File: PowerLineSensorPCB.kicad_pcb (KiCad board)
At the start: 4 copper layers, 120 x 42.2 mm, 246 parts, among them IC1 SKY65943-11, IC2 BQ21080YBGR, J1 SIM_Card_Shielded, J10 Conn_Coaxial, J11 Conn_Coaxial, J12 Conn_Coaxial, J13 Conn_Coaxial, J14 Conn_01x06_Pin, J15 Conn_01x03_MountingPin, J16 Conn_01x03_MountingPin, J17 Conn_01x03_MountingPin, J2 Micro_SD_Card, J3 Conn_Coaxial, J5 Conn_01x04_Pin, J6 USB_C_Receptacle_USB2.0_16P, J7 Conn_Coaxial, J8 Conn_01x04_Pin, SW1 SW_Push, SW2 SW_Push, SW3 SW_Push, U11 LM2903, U12 W25Q128JVE, U13 W25Q128JVE, U3 RP2350A, U5 TMAG5253BAx, U6 nRF9151-LAXX, U7 LIS2HH12, U8 RAK3172-xx-8-SM-xI, Y1 Crystal_GND24

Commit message: Update PowerLineSensorPCB and nRF9151 schematic with designator adjustments and new GND symbol
- Modified the used designators in PowerLineSensorPCB to include an additional power reference.
- Renamed the sheet in PowerLineSensorPCB for clarity.
- Removed unnecessary junctions and adjusted wire connections in nRF9151 schematic for improved layout.
- Added a new GND symbol in nRF9151 schematic to create a global label for ground.
- Adjusted positions of several components and properties for better alignment and readability.
- Updated subproject commit reference for kicad-libs.
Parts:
- AE1: footprint robots4green:W3216 -> BC_RF:W3216
- ANT1: moved to B.Cu
- moved C32 221.2 mm to (236.1, 125.3)
- moved R131 221.2 mm to (236.1, 113.8)
- moved R138 221.2 mm to (266.4, 104.0)
- moved R60 221.2 mm to (245.7, 126.9)
- moved J1 191.0 mm to (183.2, 139.6), turned to 0 degrees
- moved R114 189.8 mm to (193.2, 127.3)
- moved R113 189.0 mm to (193.2, 123.4)
- moved R115 188.6 mm to (193.2, 126.3)
- moved C26 186.0 mm to (190.4, 130.3), turned to 90 degrees
- moved C28 183.5 mm to (189.4, 130.3), turned to 90 degrees
- moved C27 183.4 mm to (188.4, 130.3), turned to 90 degrees
- moved R121 182.9 mm to (193.2, 121.4)
- moved R122 182.5 mm to (193.2, 122.4)
- moved R123 182.5 mm to (193.2, 124.3)
- moved C41 181.7 mm to (172.2, 126.4), turned to 180 degrees
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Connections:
- C26 pad 2: Net-(C26-Pad2) -> GND
- C27 pad 2: Net-(C26-Pad2) -> GND
- C28 pad 2: Net-(C26-Pad2) -> GND
- C29 pad 2: Net-(C26-Pad2) -> GND
- C40 pad 2: Net-(C26-Pad2) -> GND
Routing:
- net GND: track 10.9 -> 0.01 mm
- net Net-(U8-RF): track 12.3 -> 6.51 mm
- net Net-(ANT1-FEED): track 14.1 -> 9.50 mm, vias 0 -> 1
- net Net-(C33-Pad1): track 3.25 -> 0.00 mm
- net Net-(J7-In): track 3.06 -> 0.00 mm
- net Net-(U6-ANT): track 2.31 -> 0.00 mm
- net Net-(D9-A2): track 18.3 -> 19.2 mm
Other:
- board size 120 x 42.2 mm -> 115 x 47 mm

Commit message: general improvments
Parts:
- removed C40: 4.7u, Capacitor_SMD:C_0402_1005Metric
- added R100: 100R, Resistor_SMD:R_0402_1005Metric, F.Cu at (125.2, 90.0)
- added R99: 100R, Resistor_SMD:R_0402_1005Metric, F.Cu at (130.1, 90.0)
- C24, C29, C31, C32, C36: value 4.7u -> 4u7; footprint Capacitor_SMD:C_0402_1005Metric -> Capacitor_SMD:C_1206_3216Metric
- C28: footprint Capacitor_SMD:C_0402_1005Metric -> Capacitor_SMD:C_1206_3216Metric
- U1: value ~ -> MLX90637
- U2: value ~ -> ZTPD2210
- U4: value ~ -> RT6150BGQW
- U9: value ~ -> P3T1755
- moved R90 96.2 mm to (162.6, 121.8)
- moved U9 82.1 mm to (141.8, 122.6), turned to 180 degrees
- moved R52 80.6 mm to (146.6, 123.8)
- moved R53 80.6 mm to (146.6, 122.8)
- moved C20 77.1 mm to (138.0, 123.0), turned to 90 degrees
- moved R50 25.9 mm to (165.0, 106.6), turned to 180 degrees
- moved R51 25.5 mm to (165.0, 105.4), turned to 180 degrees
- moved R21 9.88 mm to (88.4, 153.9)
- moved R25 9.88 mm to (91.3, 153.9)
- moved C21 9.88 mm to (85.5, 159.8)
- moved R20 9.88 mm to (88.4, 151.9)
- moved R22 9.88 mm to (88.4, 155.9)
- moved R23 9.88 mm to (88.4, 157.9)
- moved R24 9.88 mm to (91.3, 151.9)
- moved R26 9.88 mm to (91.3, 155.9)
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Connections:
- R16 pad 1: /50Hz -> Net-(R16-Pad1)
- R25 pad 1: /50Hz -> Net-(R16-Pad1)
- U11 pad 1: /50Hz -> Net-(R16-Pad1)
- U6 pad 53: /Celluar_GNSS/PPS -> Net-(U6-COEX1)
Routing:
- net /I2C0.SDA: track 0.00 -> 58.6 mm, vias 0 -> 3
- net /I2C0.SCL: track 0.00 -> 33.8 mm
- net Net-(U9-A0): track 0.00 -> 6.80 mm
- net Net-(U2-SDA): track 0.00 -> 5.46 mm
- net Net-(U2-SCL): track 0.00 -> 5.17 mm
- net Net-(U9-SCL): track 0.00 -> 2.19 mm
- net Net-(U1-SCL): track 0.00 -> 1.33 mm
- net Net-(U1-SDA): track 0.00 -> 1.29 mm

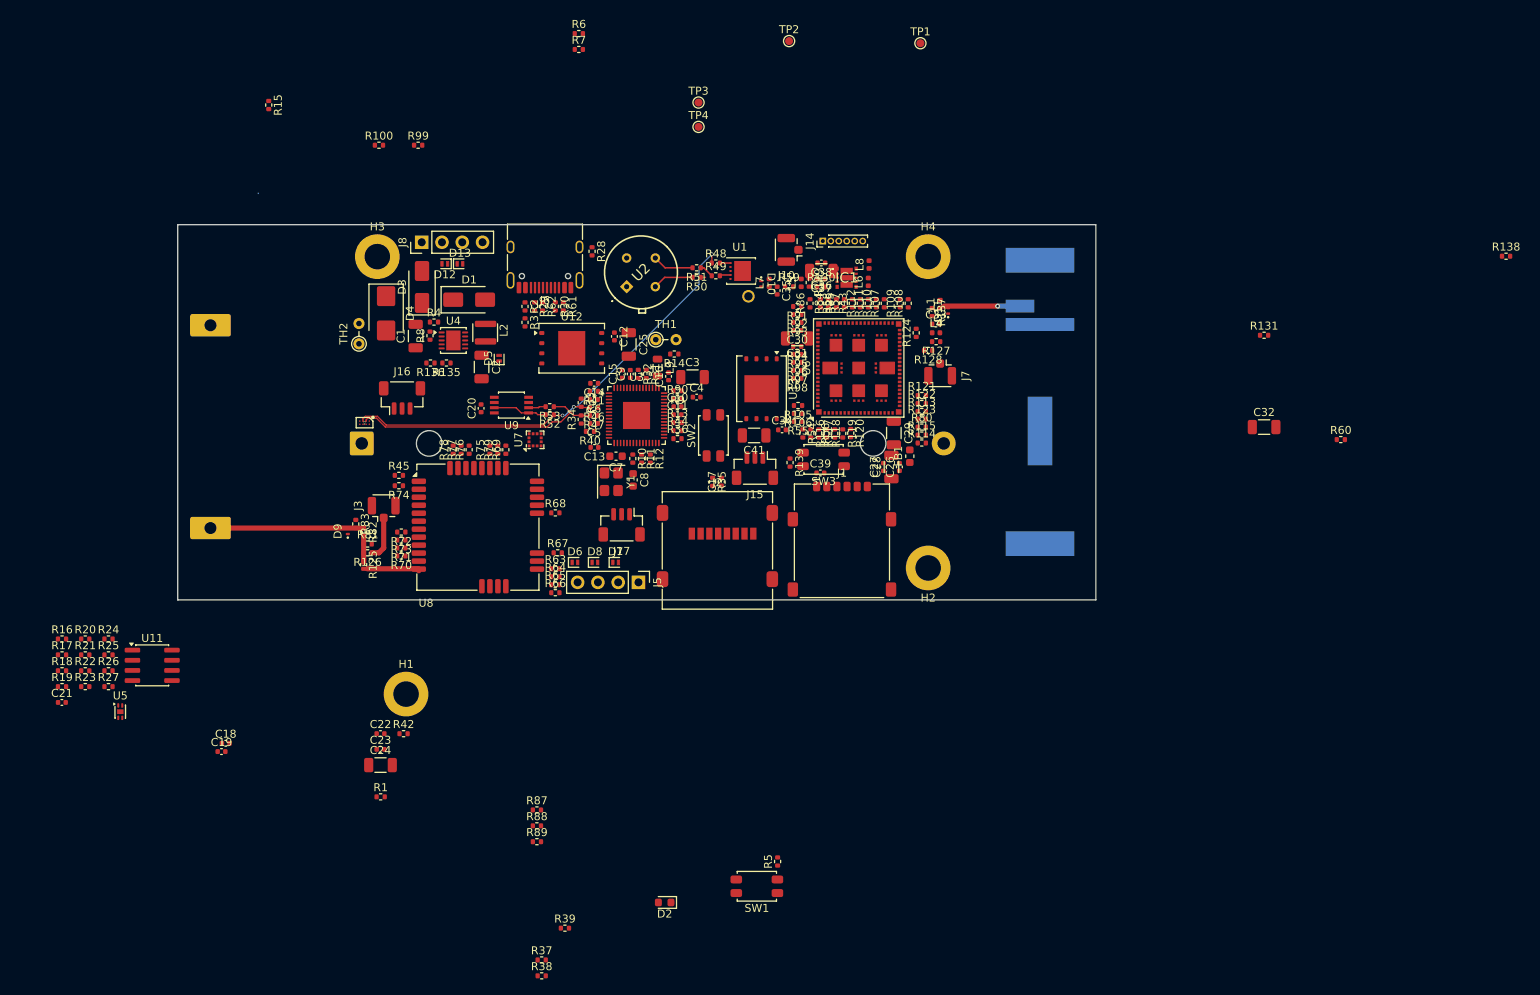
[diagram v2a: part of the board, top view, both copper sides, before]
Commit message: PCB routing.
Add netclass flags for power and signal in various schematics; update capacitor footprints and part numbers

- Introduced multiple netclass flags for "Power" and "Signal" in USB_Power, hall_effect_sensor, and nRF9151 schematics to enhance clarity and organization.
- Updated capacitor footprints from "C_1206_3216Metric" to "C_0402_1005Metric" and part numbers from "1206B475K500NT" to "CL05A475MP5NRNC" in accelerometer and nRF9151 schematics for consistency and accuracy.
- Updated submodule reference in kicad-libs to ensure compatibility with the latest library changes.
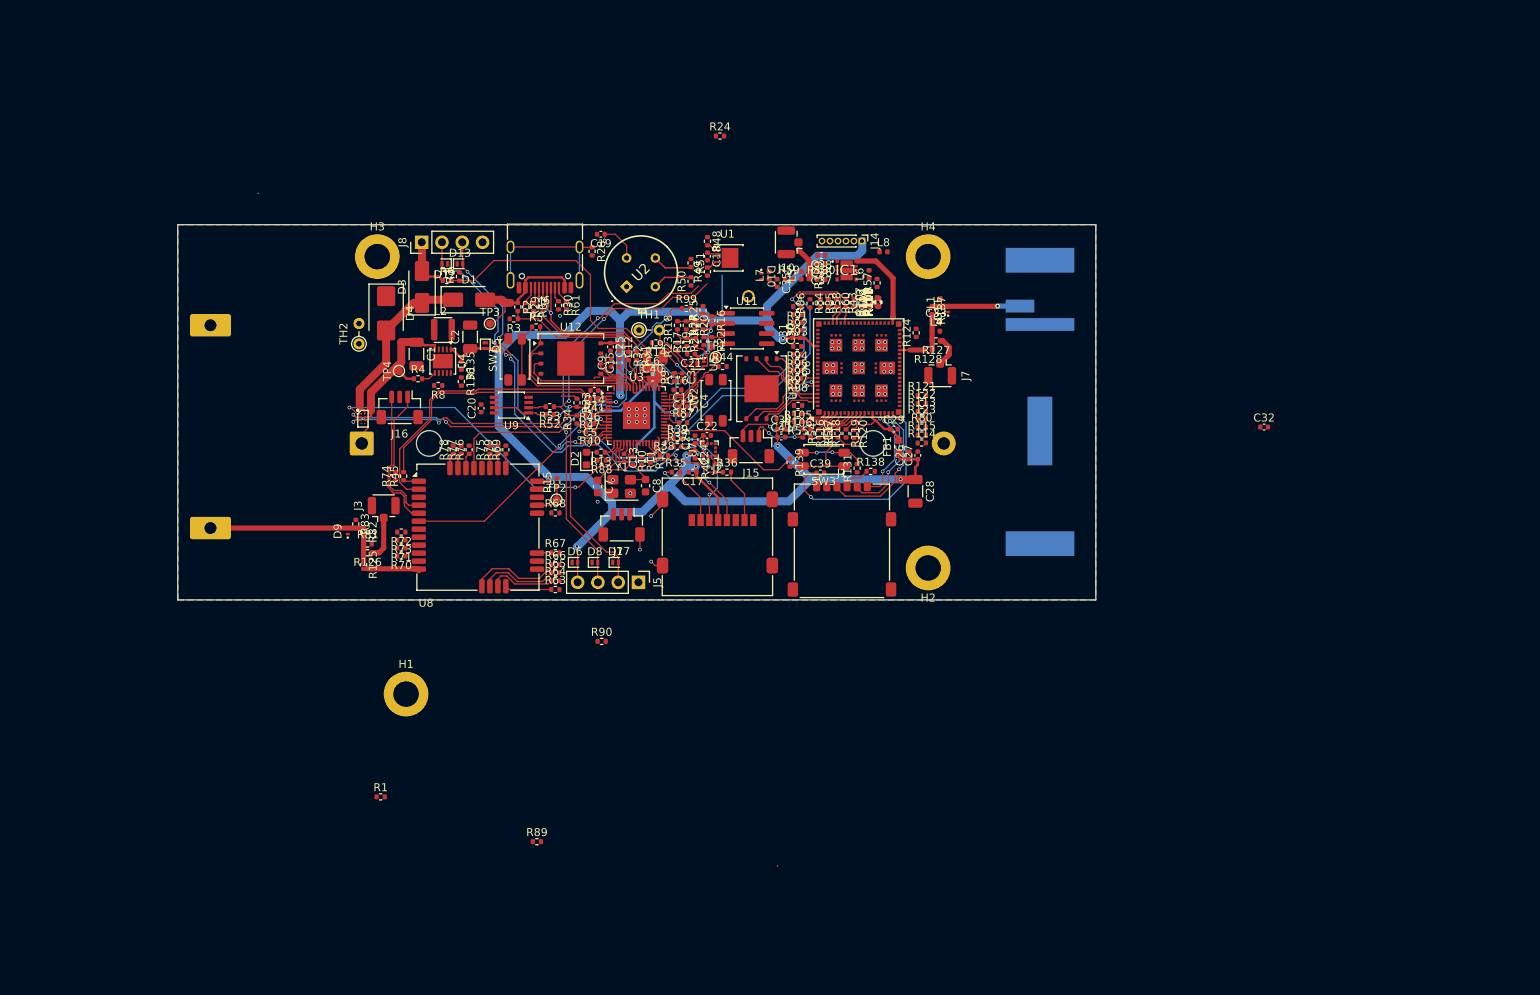
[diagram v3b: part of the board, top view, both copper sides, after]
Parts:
- added C40: 4u7, Capacitor_SMD:C_0402_1005Metric, F.Cu at (159.5, 119.2)
- C24, C25, C29, C3, C31, C32, C36, C41: footprint Capacitor_SMD:C_1206_3216Metric -> Capacitor_SMD:C_0402_1005Metric
- C6: value 100n -> 4u7
- L9: footprint Inductor_SMD:L_0805_2012Metric -> BC_Miscellaneous:AOTA-B201610S3R3-101-T
- moved R24 99.2 mm to (167.9, 88.9)
- moved R16 90.6 mm to (166.9, 112.0), turned to -90 degrees
- moved R19 90.3 mm to (164.9, 114.7), turned to 90 degrees
- moved C21 90.1 mm to (164.3, 116.2), turned to 180 degrees
- moved R22 88.7 mm to (166.9, 114.6), turned to -90 degrees
- moved R18 88.4 mm to (162.6, 112.6), turned to 90 degrees
- moved R17 87.5 mm to (163.8, 114.7), turned to 90 degrees
- moved R27 87.2 mm to (165.8, 112.6), turned to 90 degrees
- moved R21 86.9 mm to (165.9, 114.6), turned to 90 degrees
- moved R25 86.1 mm to (165.8, 110.7), turned to 90 degrees
- moved R20 85.9 mm to (164.8, 112.6), turned to -90 degrees
- moved C18 85.8 mm to (166.3, 104.0), turned to -90 degrees
- moved U11 85.6 mm to (171.3, 113.0)
- moved R23 85.5 mm to (162.6, 115.3), turned to 90 degrees
- moved U5 84.4 mm to (165.1, 117.5), turned to -90 degrees
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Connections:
- R13 pad 1: Net-(U3-GPIO25) -> Net-(U3-GPIO12)
- U3 pad 16: /RP_pico/U1 -> Net-(U3-GPIO12)
- U3 pad 37: Net-(U3-GPIO25) -> /RP_pico/U1
- U3 pad 41: /hall effect sensor/Out -> /sens1
- U3 pad 42: /sens1 -> /hall effect sensor/Out
- U3 pad 43: /RP_pico/U4 -> /RP_pico/EN_hall
- U3 pad 9: /RP_pico/EN_hall -> /RP_pico/U4
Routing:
- net +3.3V: track 0.00 -> 256.2 mm, vias 0 -> 14
- net /Celluar_GNSS/GNSS.TX: track 0.00 -> 53.2 mm, vias 0 -> 2
- net /Celluar_GNSS/GNSS.RX: track 0.00 -> 52.7 mm, vias 0 -> 2
- net /I2C0.SCL: track 33.8 -> 86.0 mm, vias 0 -> 4
- net /50Hz: track 0.00 -> 51.8 mm, vias 0 -> 3
- net Power_ext: track 0.00 -> 49.6 mm, vias 0 -> 2
- net ~{INT}_Battery_Charger: track 0.00 -> 43.3 mm, vias 0 -> 2
- net /Power/EXT_PWR.TX: track 0.00 -> 41.3 mm, vias 0 -> 4
- net /Power/EXT_PWR.RX: track 0.00 -> 39.0 mm, vias 0 -> 4
- net /LORA/LORA.TX: track 0.00 -> 35.8 mm
- net /LORA/LORA.RX: track 0.00 -> 34.0 mm
- net +1V1: track 0.00 -> 32.6 mm, vias 0 -> 5
- net Power_usb: track 0.00 -> 32.5 mm, vias 0 -> 1
- net /Celluar_GNSS/SIM_1V8: track 0.00 -> 29.4 mm, vias 0 -> 2
- net /I2C0.SDA: track 58.6 -> 84.3 mm, vias 3 -> 6
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- added copper zone on F.Cu, net +3.3V
- added copper zone on B.Cu, net GND
- added copper zone on F.Cu, net GND
- added copper zone on In1.Cu, net GND
- added copper zone on In2.Cu, net GND
- added copper zone on F.Cu, net Net-(U3-VREG_LX)

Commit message: pcb edits. remove old backups
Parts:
- removed H1: MountingHole_Pad, MountingHole:MountingHole_3.2mm_M3_DIN965_Pad
- added C42: 100n, Capacitor_SMD:C_0402_1005Metric, F.Cu at (175.6, 111.6)
- J11, J12, J13, R132, R133, R134, TP1: moved to B.Cu
- moved R134 112.4 mm to (185.6, 142.6), turned to 0 degrees
- moved R133 104.5 mm to (172.0, 142.6)
- moved J13 103.1 mm to (176.6, 142.6)
- moved J12 99.1 mm to (163.0, 142.6), turned to 180 degrees
- moved R132 78.1 mm to (145.2, 142.8)
- moved J11 73.1 mm to (136.2, 142.9), turned to 180 degrees
- moved R1 69.9 mm to (168.8, 116.9)
- moved R89 54.6 mm to (163.3, 125.8)
- moved C32 40.4 mm to (195.7, 123.4)
- moved R24 27.2 mm to (166.7, 116.1)
- moved R90 26.0 mm to (149.9, 126.4), turned to 90 degrees
- moved TP1 6.10 mm to (162.4, 113.1), turned to 180 degrees
- moved R15 5.28 mm to (148.2, 137.5), turned to -90 degrees
- moved C39 4.15 mm to (176.3, 131.1), turned to 180 degrees
- moved J14 3.42 mm to (189.1, 101.7)
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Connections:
- J15 pad 1: /Celluar_GNSS/SD -> /Celluar_GNSS/SC
- J15 pad 3: /Celluar_GNSS/SC -> /Celluar_GNSS/SD
- R14 pad 1: /RP_pico/A0 -> /RP_pico/A3
- R23 pad 1: /RP_pico/EN_hall -> /RP_pico/A2
- TH1 pad 2: /RP_pico/A0 -> /RP_pico/A3
- U3 pad 40: /RP_pico/A0 -> /sens1
- U3 pad 41: /sens1 -> /hall effect sensor/Out
- U3 pad 42: /hall effect sensor/Out -> /RP_pico/A2
- U3 pad 43: /RP_pico/EN_hall -> /RP_pico/A3
- U5 pad 3: /RP_pico/EN_hall -> /RP_pico/A2
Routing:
- net +3.3V: track 256.2 -> 320.7 mm, vias 14 -> 22
- net /Celluar_GNSS/PPS: track 24.5 -> 66.8 mm, vias 2 -> 6
- net Pulse_Switch_converter: track 0.00 -> 26.4 mm, vias 0 -> 2
- net GND: track 6.26 -> 27.9 mm, vias 55 -> 405
- net LORA_~{RST}: track 0.00 -> 21.4 mm, vias 0 -> 4
- net /Celluar_GNSS/U4: track 0.00 -> 19.1 mm, vias 0 -> 1
- net /Celluar_GNSS/U2: track 0.00 -> 19.0 mm, vias 0 -> 1
- net /Celluar_GNSS/U3: track 0.00 -> 18.4 mm, vias 0 -> 1
- net /RP_pico/RUN: track 0.00 -> 17.5 mm, vias 0 -> 2
- net /Celluar_GNSS/U1: track 0.00 -> 16.7 mm, vias 0 -> 1
- net /Celluar_GNSS/COEX0: track 0.00 -> 14.7 mm, vias 0 -> 2
- net /RP_pico/A3: track 0.00 -> 13.1 mm
- net Net-(IC2-TS/MR): track 0.00 -> 13.0 mm
- net Net-(J17-Pin_3): track 0.00 -> 12.1 mm
- net /RP_pico/A2: track 0.00 -> 9.90 mm
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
